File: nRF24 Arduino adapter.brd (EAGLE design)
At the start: 22.5 x 15.2 mm, 4 parts

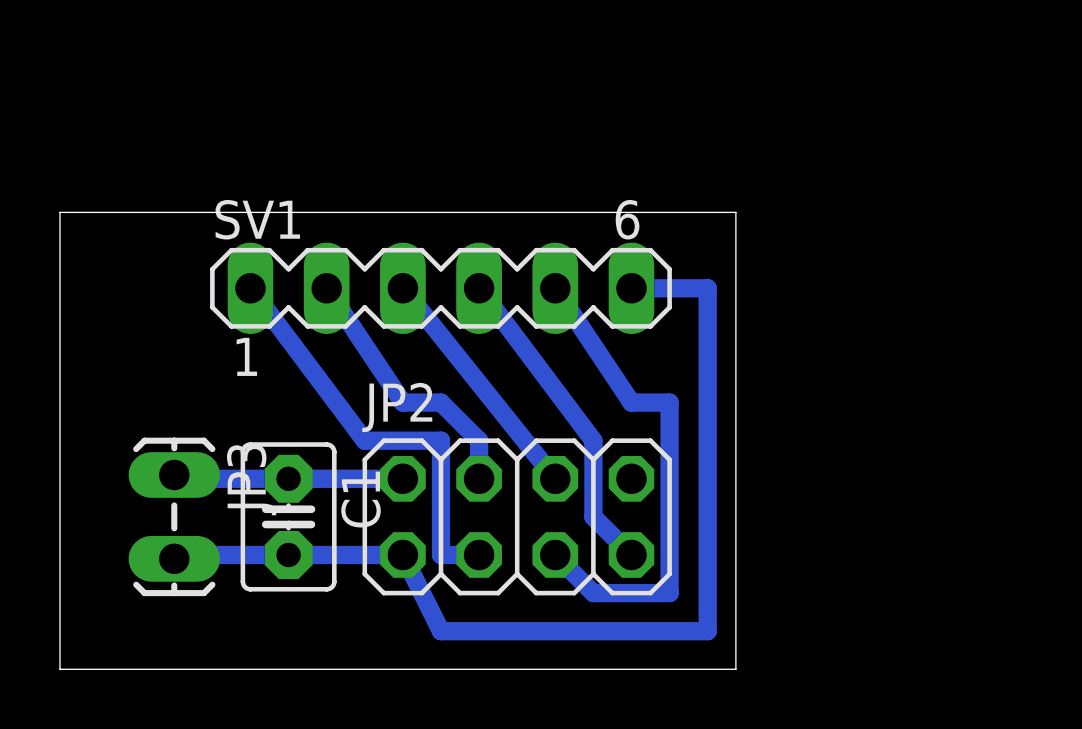
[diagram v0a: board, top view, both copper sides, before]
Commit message: New version of schema
Thanks to Rikard "Ornotermes" Lindström for the help
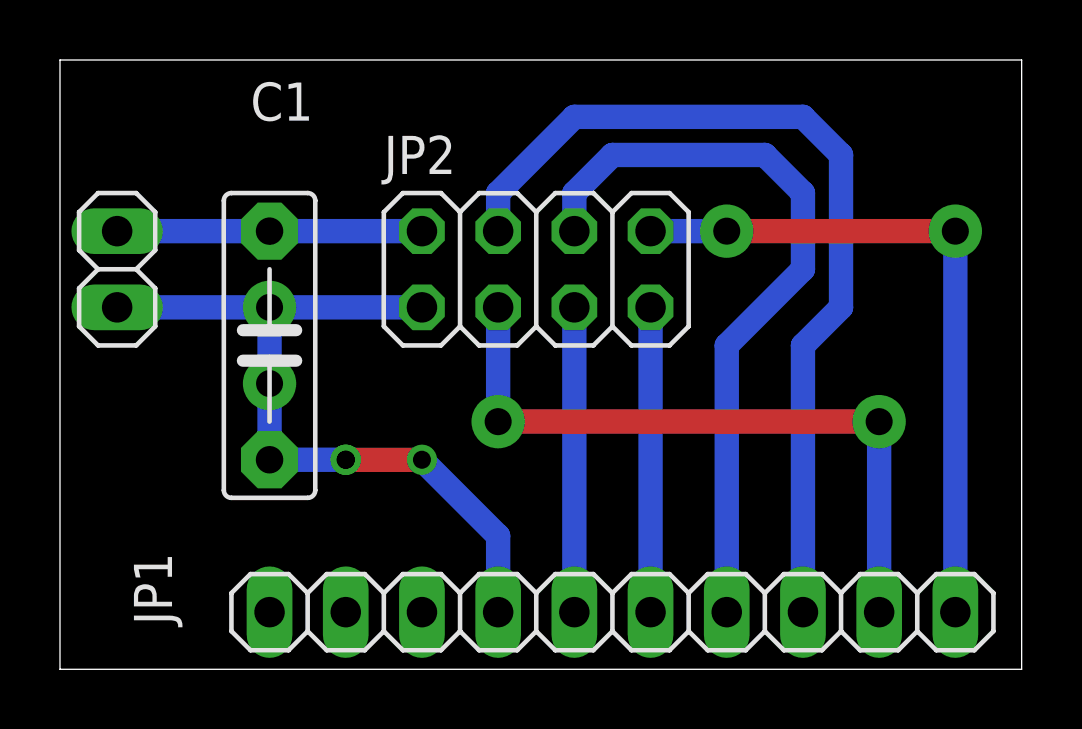
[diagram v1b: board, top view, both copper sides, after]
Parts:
- removed SV1: (no value), con-lstb:MA06-1
- added JP1: (no value), pinhead:1X10
- C1: value (none) -> 100n; device capacitor-wima:C2.5-3 -> capacitor-wima:C7.5B3
- JP3: value Power -> (none); device SparkFun-Connectors:1X02_LOCK_LONGPADS -> pinhead:1X02
- moved JP2 8.28 mm to (15.9, 13.3)
- moved JP3 7.24 mm to (1.91, 13.3)
- moved C1 5.75 mm to (6.99, 10.8)
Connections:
- net N$3 renamed +3V3
- removed net N$1: C1.2, JP2.1, JP3.2, SV1.6
- removed net N$2: JP2.3, SV1.1
- removed net N$4: JP2.4, SV1.2
- removed net N$5: JP2.6, SV1.3
- removed net N$6: JP2.5, SV1.5
- removed net N$8: JP2.7, SV1.4
- new net CE: JP1.2, JP2.3
- new net CSN: JP1.3, JP2.4
- new net GND: C1.2, JP1.7, JP2.1, JP3.2
- new net IRQ: JP1.1, JP2.8
- new net MISO: JP1.5, JP2.7
- new net MOSI: JP1.4, JP2.6
- new net SCK: JP1.6, JP2.5
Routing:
- net N$1: track 33.4 -> 0.00 mm
- net CSN: track 0.00 -> 30.0 mm
- net GND: track 0.00 -> 26.5 mm, vias 0 -> 5
- net MOSI: track 0.00 -> 25.0 mm
- net IRQ: track 0.00 -> 22.9 mm, vias 0 -> 2
- net CE: track 0.00 -> 22.9 mm, vias 0 -> 2
- net N$6: track 16.5 -> 0.00 mm
- net N$2: track 14.0 -> 0.00 mm
- net N$8: track 10.7 -> 0.00 mm
- net SCK: track 0.00 -> 10.2 mm
- net MISO: track 0.00 -> 10.2 mm
- net N$4: track 8.92 -> 0.00 mm
- net N$5: track 8.13 -> 0.00 mm
- net +3V3: track 7.75 -> 10.2 mm, vias 1 -> 0
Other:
- board size 22.5 x 15.2 mm -> 32.1 x 20.3 mm
- board text added: "+"
- board text added: "-"
- board text added: "3V3"
- board text added: "D10"
- board text added: "D11"
- board text added: "D12"
- board text added: "D13"
- board text added: "D8"
- board text added: "D9"
- board text added: "GND"
